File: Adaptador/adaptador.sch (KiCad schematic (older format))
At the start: 3 parts, among them P1 CONN_02X06, P2 CONN_01X03, U1 MCP3002

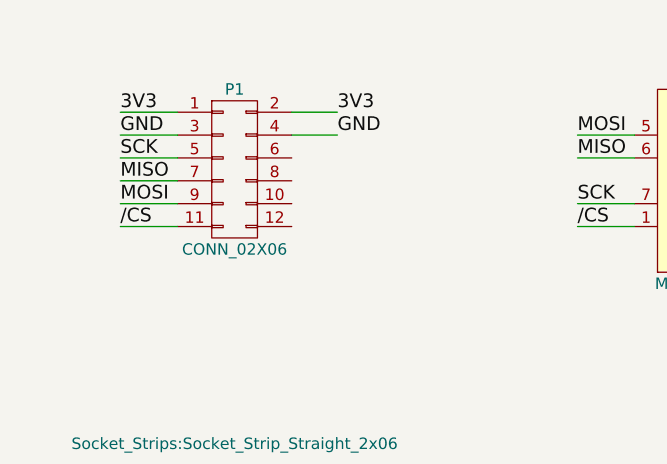
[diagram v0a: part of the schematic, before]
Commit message: Canvis a la PCB. No puc dormir sino. Crec que ara esta be (el coure queda a la vista cap a dalt i tot es munta per baix
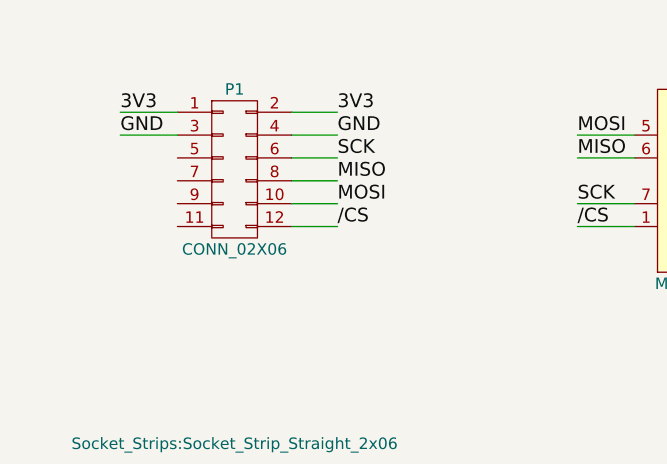
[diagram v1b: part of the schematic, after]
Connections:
- net /CS: now also P1.12 (P12); no longer P1.11 (P11)
- net MISO: now also P1.8 (P8); no longer P1.7 (P7)
- net MOSI: now also P1.10 (P10); no longer P1.9 (P9)
- net SCK: now also P1.6 (P6); no longer P1.5 (P5)
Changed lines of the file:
@@
 LIBS:contrib
 LIBS:valves
+LIBS:adaptador-cache
 EELAYER 25 0
 EELAYER END
@@
 Text Label 1800 3100 0    60   ~ 0
 GND
-Text Label 1800 3200 0    60   ~ 0
+Text Label 2750 3200 0    60   ~ 0
 SCK
-Text Label 1800 3300 0    60   ~ 0
+Text Label 2750 3300 0    60   ~ 0
 MISO
 Wire Wire Line
@@
 	-1   0    0    1
 $EndComp
-Text Label 1800 3500 0    60   ~ 0
+Text Label 2750 3500 0    60   ~ 0
 /CS
-Text Label 1800 3400 0    60   ~ 0
+Text Label 2750 3400 0    60   ~ 0
 MOSI
 Wire Wire Line
@@
 	1800 3000 2050 3000
 Wire Wire Line
-	1800 3500 2050 3500
+	2550 3200 2750 3200
 Wire Wire Line
-	2050 3400 1800 3400
+	2550 3300 2750 3300
 Wire Wire Line
-	1800 3300 2050 3300
+	2750 3400 2550 3400
 Wire Wire Line
-	1800 3200 2050 3200
+	2550 3500 2750 3500
 $EndSCHEMATC
